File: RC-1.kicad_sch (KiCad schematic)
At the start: 50 parts, among them J1 U.FL, P1 PCIe_M.2_B-Key, U1 STM32F401CEUx, U2 ADF7021, X1 TCXO, Y1 8MHz, Y2 32KHz

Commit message: Set project title and add PDF schematic
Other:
- company: (none) -> OpenRTX + M17
- title: (none) -> Radio Card RC-1
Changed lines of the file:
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@@
 (kicad_sch (version 20211123) (generator eeschema)
   (paper "A4")
+  (title_block
+    (title "Radio Card RC-1")
+    (date "2021-12-29")
+    (rev "d4f4755")
+    (company "OpenRTX + M17")
+  )
   (junction (at 157.48 171.45) (diameter 0) (color 0 0 0 0)
   )

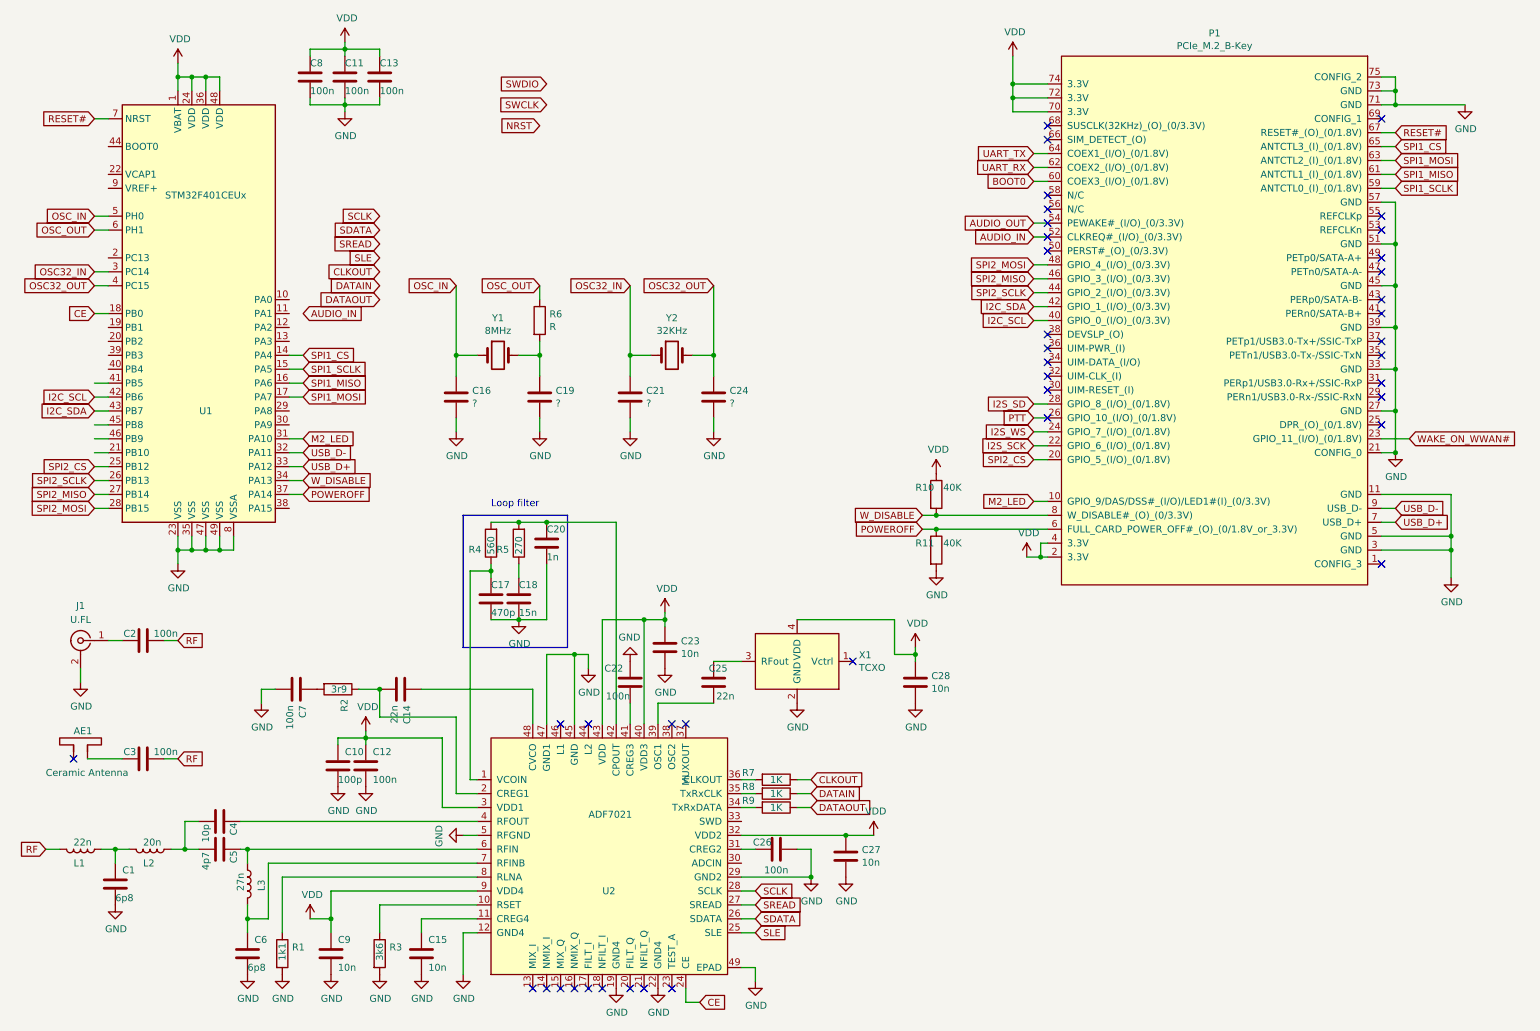
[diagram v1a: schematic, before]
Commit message: Split schematic into 3 sheets: connectors, mcu and radio
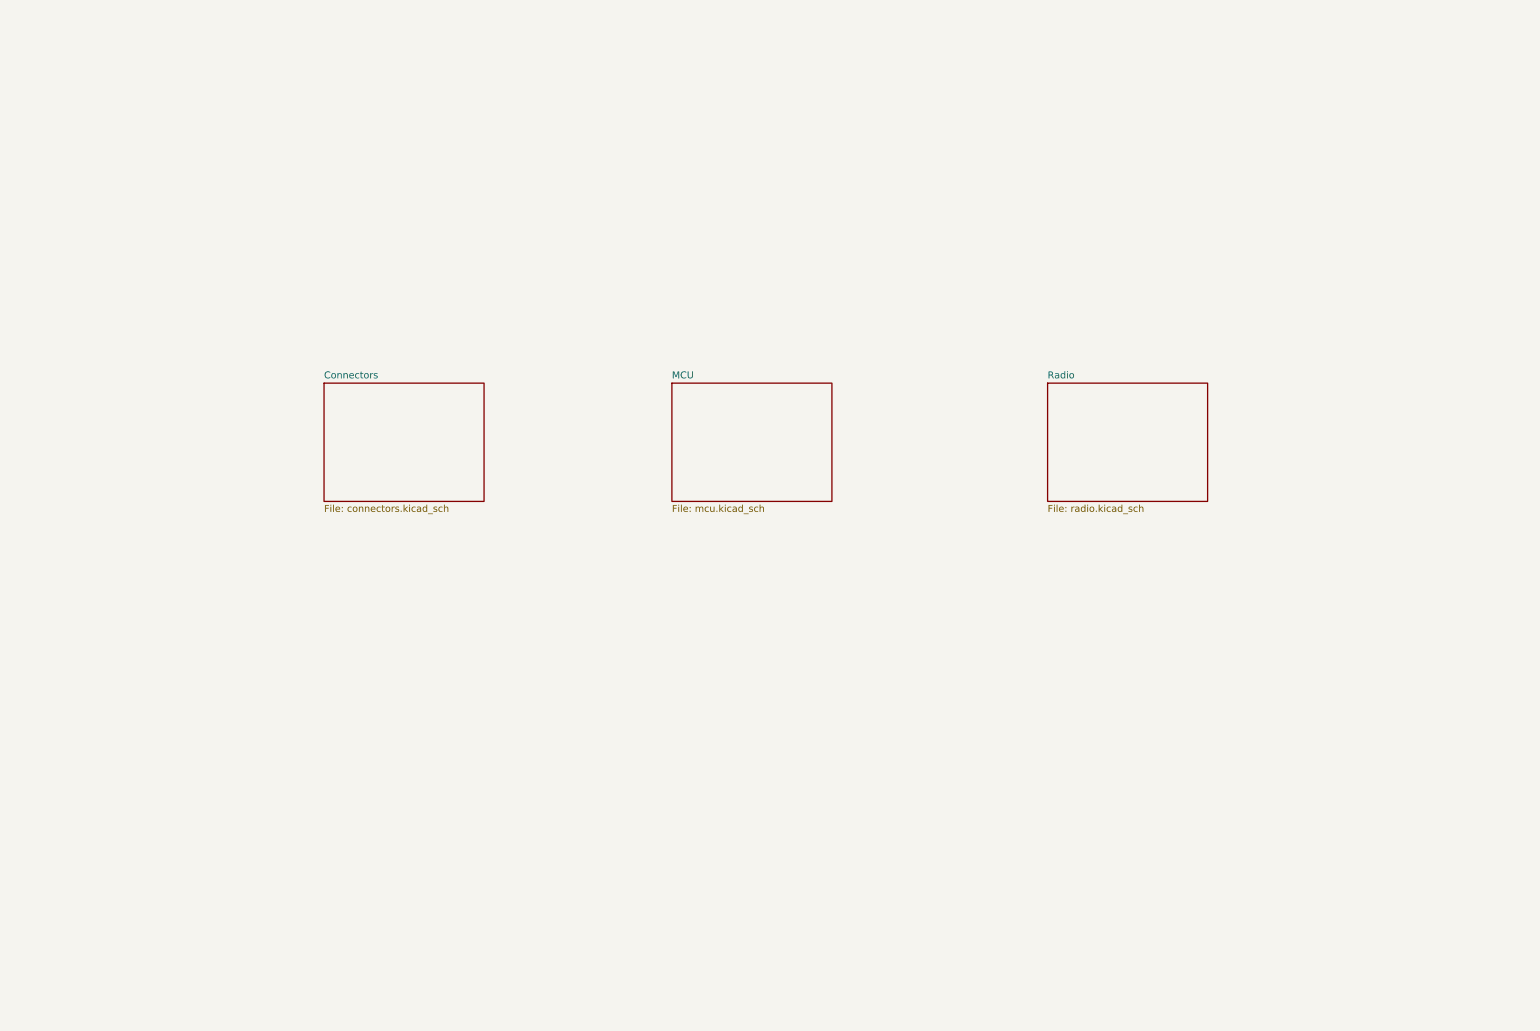
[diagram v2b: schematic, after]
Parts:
- removed AE1: Ceramic Antenna, symbol Device:Antenna_Dipole
- removed C1, C6: 6p8, Capacitor_SMD:C_0402_1005Metric, symbol Device:C
- removed C10: 100p, Capacitor_SMD:C_0402_1005Metric, symbol Device:C
- removed C11, C12, C13, C2, C22, C26, C3, C7, C8: 100n, Capacitor_SMD:C_0402_1005Metric, symbol Device:C
- removed C14, C25: 22n, Capacitor_SMD:C_0402_1005Metric, symbol Device:C
- removed C15, C23, C27, C28, C9: 10n, Capacitor_SMD:C_0402_1005Metric, symbol Device:C
- removed C16, C19, C21, C24: ?, Capacitor_SMD:C_0402_1005Metric, symbol Device:C
- removed C17: 470p, Capacitor_SMD:C_0402_1005Metric, symbol Device:C
- removed C18: 15n, Capacitor_SMD:C_0402_1005Metric, symbol Device:C
- removed C20: 1n, Capacitor_SMD:C_0402_1005Metric, symbol Device:C
- removed C4: 10p, Capacitor_SMD:C_0402_1005Metric, symbol Device:C
- removed C5: 4p7, Capacitor_SMD:C_0402_1005Metric, symbol Device:C
- removed J1: U.FL, Connector_Coaxial:U.FL_Hirose_U.FL-R-SMT-1_Vertical, symbol Connector:Conn_Coaxial
- removed L1: 22n, Inductor_SMD:L_0402_1005Metric, symbol Device:L
- removed L2: 20n, Inductor_SMD:L_0402_1005Metric, symbol Device:L
- removed L3: 27n, Inductor_SMD:L_0402_1005Metric, symbol Device:L
- removed P1: PCIe_M.2_B-Key, NGFF:NGFF_B, symbol PCIe_M.2:PCIe_M.2_B-Key
- removed R1: 1k1, Resistor_SMD:R_0402_1005Metric, symbol Device:R
- removed R10, R11: 40K, Resistor_SMD:R_0402_1005Metric, symbol Device:R
- removed R2: 3r9, Resistor_SMD:R_0402_1005Metric, symbol Device:R
- removed R3: 3k6, Resistor_SMD:R_0402_1005Metric, symbol Device:R
- removed R4: 560, Resistor_SMD:R_0402_1005Metric, symbol Device:R
- removed R5: 270, Resistor_SMD:R_0402_1005Metric, symbol Device:R
- removed R6: R, Resistor_SMD:R_01005_0402Metric, symbol Device:R
- removed R7, R8, R9: 1K, Resistor_SMD:R_0402_1005Metric, symbol Device:R
- removed U1: STM32F401CEUx, Package_DFN_QFN:QFN-48-1EP_7x7mm_P0.5mm_EP5.6x5.6mm, symbol MCU_ST_STM32F4:STM32F401CEUx
- removed U2: ADF7021, Package_CSP:LFCSP-48-1EP_7x7mm_P0.5mm_EP4.1x4.1mm, symbol adf7021:ADF7021
- removed X1: TCXO, symbol tcxo:TCXO
- removed Y1: 8MHz, symbol Device:Crystal
- removed Y2: 32KHz, symbol Device:Crystal
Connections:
- no-connect marks 41 -> 0
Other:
- added sheet Connectors (connectors.kicad_sch)
- added sheet MCU (mcu.kicad_sch)
- added sheet Radio (radio.kicad_sch)
- note removed: "Loop filter"

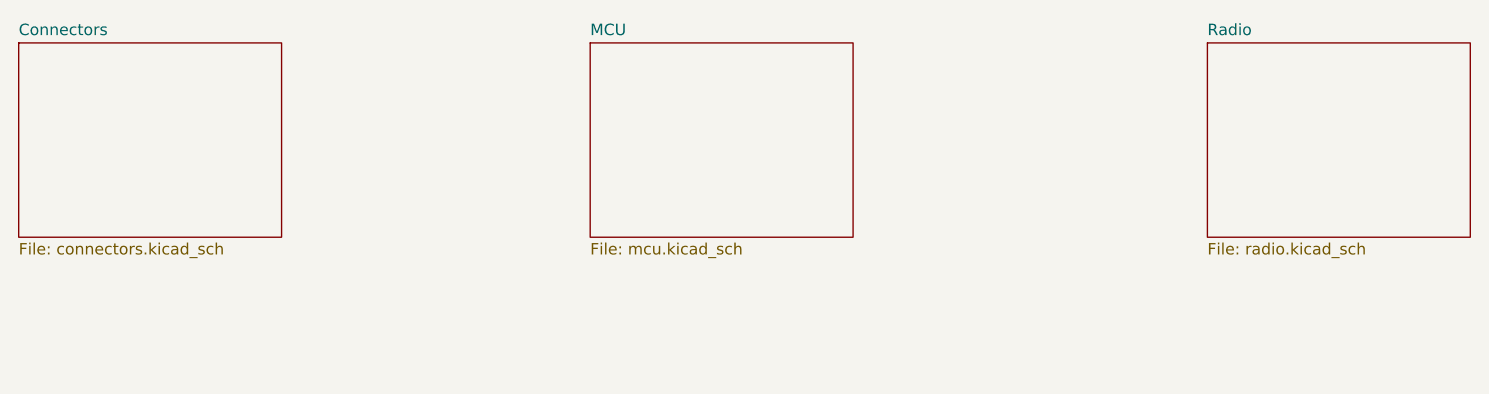
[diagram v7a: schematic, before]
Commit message: Added interfacing transistors for LED and nRESET signals on M.2 connector, switched from global to hierarchical net labels
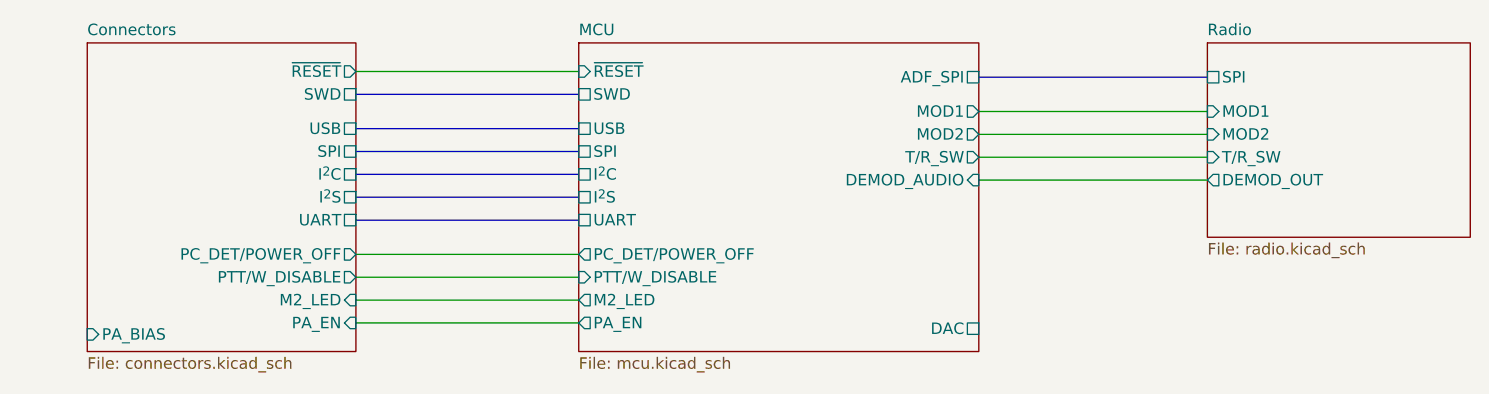
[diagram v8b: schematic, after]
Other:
- sheet Connectors ports: added I^{2}C, I^{2}S, M2_LED, PA_BIAS, PA_EN, PC_DET/POWER_OFF, PTT/W_DISABLE, SPI, SWD, UART, USB, ~{RESET}; removed none
- sheet MCU ports: added ADF_SPI, DAC, DEMOD_AUDIO, I^{2}C, I^{2}S, M2_LED, MOD1, MOD2, PA_EN, PC_DET/POWER_OFF, PTT/W_DISABLE, SPI, SWD, T/R_SW, UART, USB, ~{RESET}; removed none
- sheet Radio ports: added DEMOD_OUT, MOD1, MOD2, SPI, T/R_SW; removed none
